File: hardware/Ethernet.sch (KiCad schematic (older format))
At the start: 25 parts

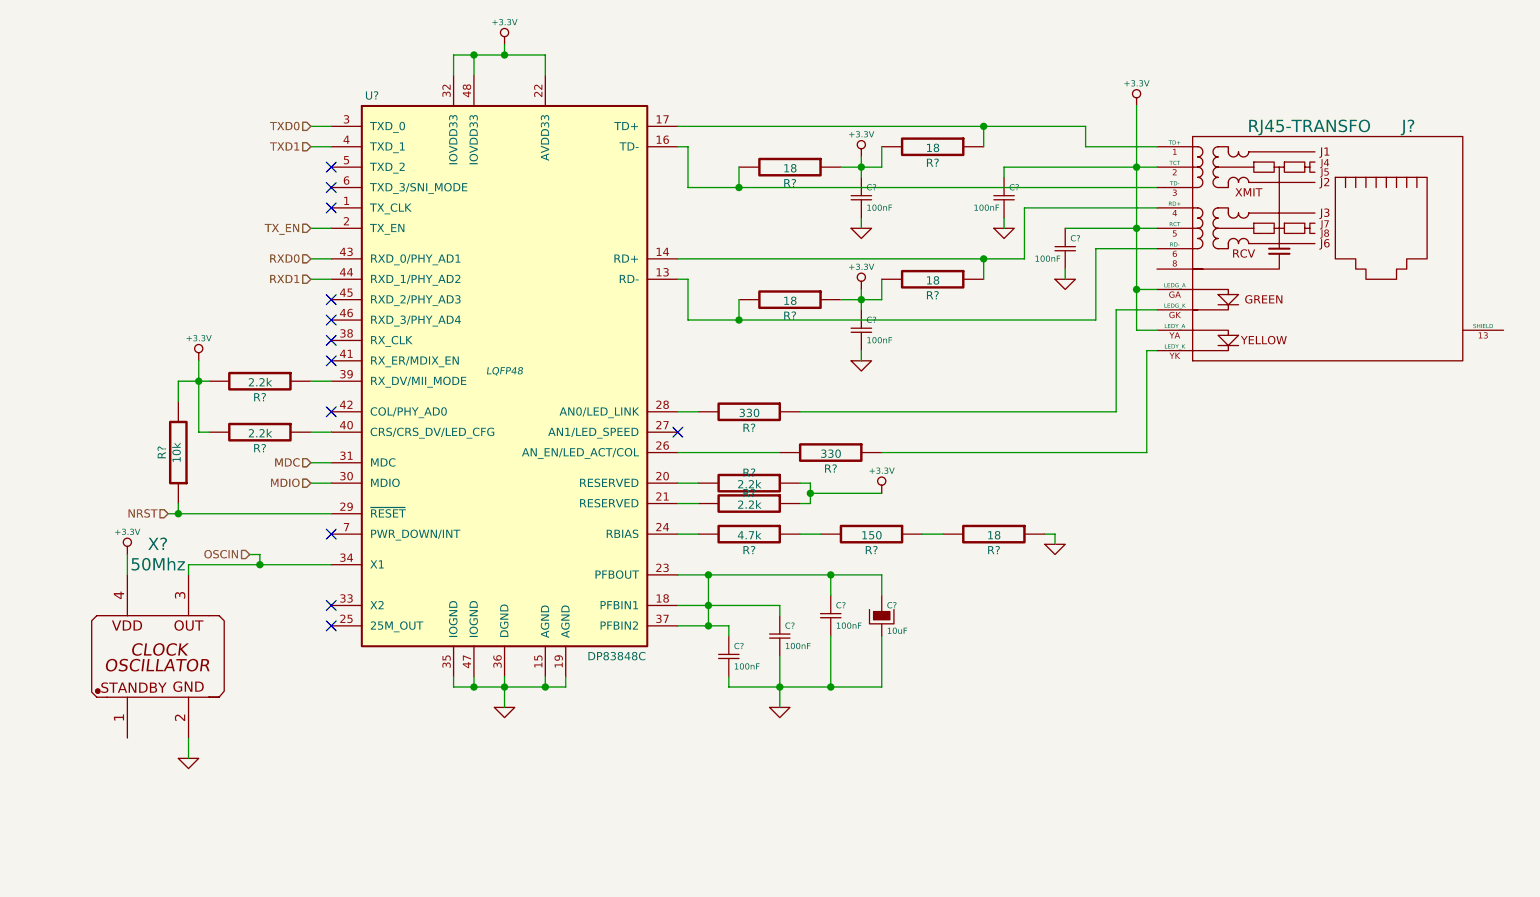
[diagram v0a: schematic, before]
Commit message: Se agrego alimentacion por USB-Serie, falta fuente
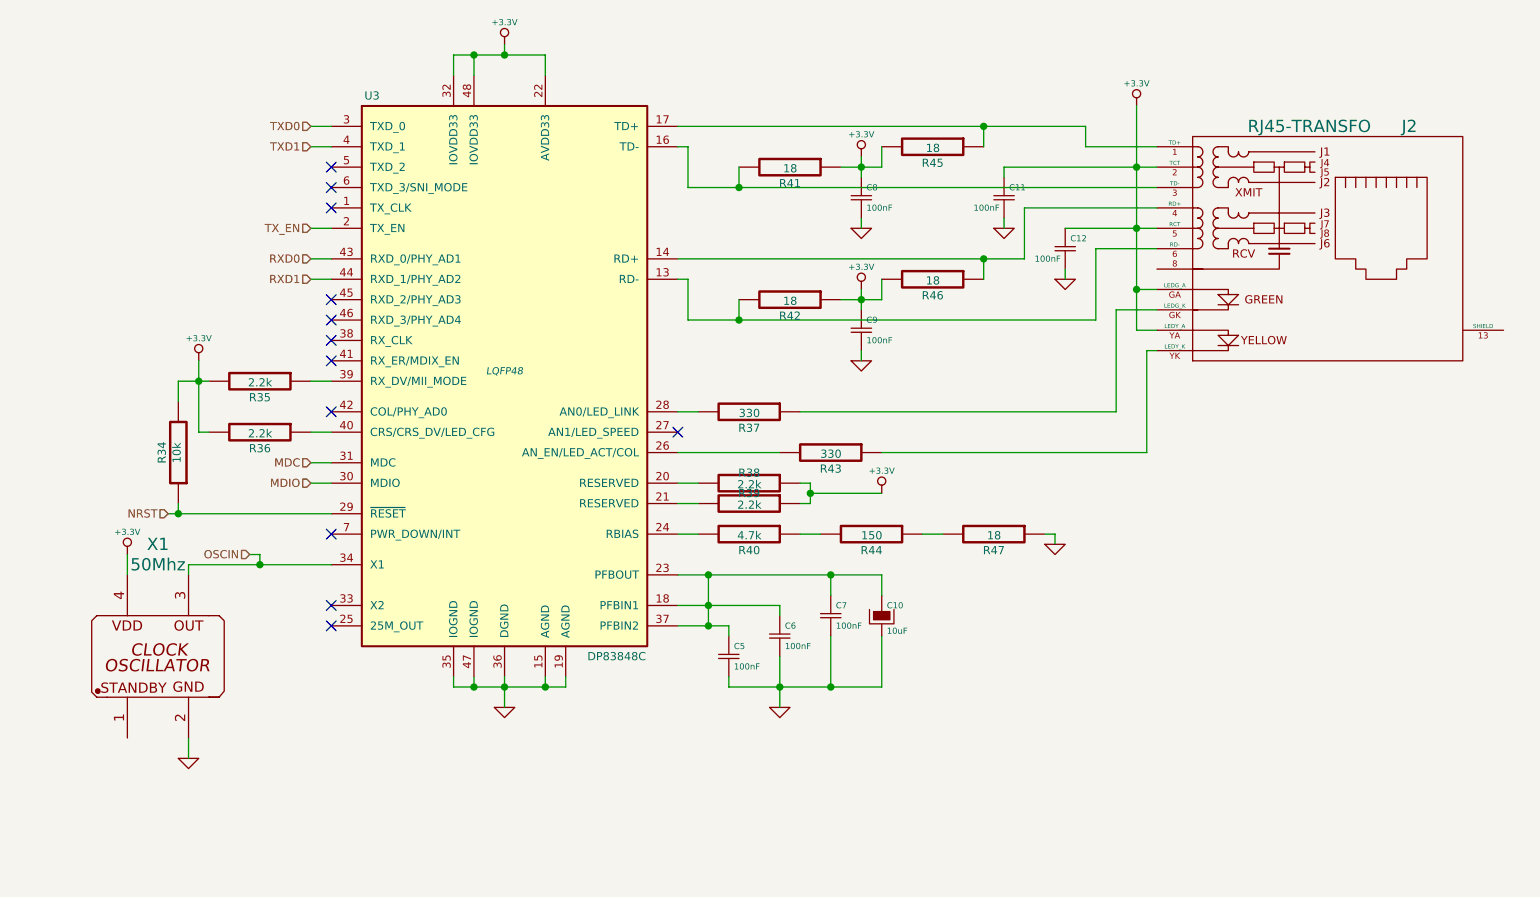
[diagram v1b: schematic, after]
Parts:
- gave numbers to parts that had none: 25
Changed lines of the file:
@@
 $Descr A4 11693 8268
 encoding utf-8
-Sheet 4 4
+Sheet 4 5
 Title ""
 Date ""
@@
 $EndDescr
 $Comp
-L DP83848C U?
+L DP83848C U3
 U 1 1 53947305
 P 4500 3600
-F 0 "U?" H 3850 4950 40  0000 C CNN
+F 0 "U3" H 3850 4950 40  0000 C CNN
 F 1 "DP83848C" H 5050 2200 40  0000 C CNN
 F 2 "LQFP48" H 4500 3600 35  0000 C CIN
@@
 $EndComp
 $Comp
-L R R?
+L R R40
 U 1 1 53947368
 P 5700 4400
-F 0 "R?" V 5780 4400 40  0000 C CNN
+F 0 "R40" V 5780 4400 40  0000 C CNN
 F 1 "4.7k" V 5707 4401 40  0000 C CNN
 F 2 "" V 5630 4400 30  0000 C CNN
@@
 $EndComp
 $Comp
-L R R?
+L R R44
 U 1 1 53947449
 P 6300 4400
-F 0 "R?" V 6380 4400 40  0000 C CNN
+F 0 "R44" V 6380 4400 40  0000 C CNN
 F 1 "150" V 6307 4401 40  0000 C CNN
 F 2 "" V 6230 4400 30  0000 C CNN
@@
 $EndComp
 $Comp
-L R R?
+L R R47
 U 1 1 53947480
 P 6900 4400
-F 0 "R?" V 6980 4400 40  0000 C CNN
+F 0 "R47" V 6980 4400 40  0000 C CNN
 F 1 "18" V 6907 4401 40  0000 C CNN
 F 2 "" V 6830 4400 30  0000 C CNN
@@
 	6550 4400 6650 4400
 $Comp
-L GND #PWR?
+L GND #PWR48
 U 1 1 539474DC
 P 7200 4450
-F 0 "#PWR?" H 7200 4450 30  0001 C CNN
+F 0 "#PWR48" H 7200 4450 30  0001 C CNN
 F 1 "GND" H 7200 4380 30  0001 C CNN
 F 2 "" H 7200 4450 60  0000 C CNN
@@
 	7200 4400 7150 4400
 $Comp
-L GND #PWR?
+L GND #PWR40
 U 1 1 53947528
 P 4500 5250
-F 0 "#PWR?" H 4500 5250 30  0001 C CNN
+F 0 "#PWR40" H 4500 5250 30  0001 C CNN
 F 1 "GND" H 4500 5180 30  0001 C CNN
 F 2 "" H 4500 5250 60  0000 C CNN
@@
 Connection ~ 4350 5150
 $Comp
-L +3.3V #PWR?
+L +3.3V #PWR39
 U 1 1 539475B5
 P 4500 2000
-F 0 "#PWR?" H 4500 1960 30  0001 C CNN
+F 0 "#PWR39" H 4500 1960 30  0001 C CNN
 F 1 "+3.3V" H 4500 2110 30  0000 C CNN
 F 2 "" H 4500 2000 60  0000 C CNN
@@
 Connection ~ 4500 2050
 $Comp
-L R R?
+L R R35
 U 1 1 5394763E
 P 3300 3650
-F 0 "R?" V 3380 3650 40  0000 C CNN
+F 0 "R35" V 3380 3650 40  0000 C CNN
 F 1 "2.2k" V 3307 3651 40  0000 C CNN
 F 2 "" V 3230 3650 30  0000 C CNN
@@
 	3550 3650 3650 3650
 $Comp
-L R R?
+L R R36
 U 1 1 539476E2
 P 3300 3900
-F 0 "R?" V 3380 3900 40  0000 C CNN
+F 0 "R36" V 3380 3900 40  0000 C CNN
 F 1 "2.2k" V 3307 3901 40  0000 C CNN
 F 2 "" V 3230 3900 30  0000 C CNN
@@
 Connection ~ 3000 3650
 $Comp
-L +3.3V #PWR?
+L +3.3V #PWR38
 U 1 1 53947762
 P 3000 3550
-F 0 "#PWR?" H 3000 3510 30  0001 C CNN
+F 0 "#PWR38" H 3000 3510 30  0001 C CNN
 F 1 "+3.3V" H 3000 3660 30  0000 C CNN
 F 2 "" H 3000 3550 60  0000 C CNN
@@
 	3550 2900 3650 2900
 $Comp
-L RJ45-TRANSFO J?
+L RJ45-TRANSFO J2
 U 1 1 539487CB
 P 8800 3000
-F 0 "J?" H 8900 3600 60  0000 L CNN
+F 0 "J2" H 8900 3600 60  0000 L CNN
 F 1 "RJ45-TRANSFO" H 8750 3600 60  0000 R CNN
 F 2 "" H 8800 3000 60  0000 C CNN
@@
 $EndComp
 $Comp
-L +3.3V #PWR?
+L +3.3V #PWR50
 U 1 1 53948AF2
 P 7600 2300
-F 0 "#PWR?" H 7600 2260 30  0001 C CNN
+F 0 "#PWR50" H 7600 2260 30  0001 C CNN
 F 1 "+3.3V" H 7600 2410 30  0000 C CNN
 F 2 "" H 7600 2300 60  0000 C CNN
@@
 	5400 2500 5350 2500
 $Comp
-L R R?
+L R R45
 U 1 1 53948C94
 P 6600 2500
-F 0 "R?" V 6680 2500 40  0000 C CNN
+F 0 "R45" V 6680 2500 40  0000 C CNN
 F 1 "18" V 6607 2501 40  0000 C CNN
 F 2 "" V 6530 2500 30  0000 C CNN
@@
 $EndComp
 $Comp
-L R R?
+L R R41
 U 1 1 53948D6C
 P 5900 2600
-F 0 "R?" V 5980 2600 40  0000 C CNN
+F 0 "R41" V 5980 2600 40  0000 C CNN
 F 1 "18" V 5907 2601 40  0000 C CNN
 F 2 "" V 5830 2600 30  0000 C CNN
@@
 Connection ~ 6850 2400
 $Comp
-L +3.3V #PWR?
+L +3.3V #PWR42
 U 1 1 53949005
 P 6250 2550
-F 0 "#PWR?" H 6250 2510 30  0001 C CNN
+F 0 "#PWR42" H 6250 2510 30  0001 C CNN
 F 1 "+3.3V" H 6250 2660 30  0000 C CNN
 F 2 "" H 6250 2550 60  0000 C CNN
@@
 $EndComp
 $Comp
-L Csmall C?
+L Csmall C8
 U 1 1 5394905D
 P 6250 2750
-F 0 "C?" H 6275 2800 30  0000 L CNN
+F 0 "C8" H 6275 2800 30  0000 L CNN
 F 1 "100nF" H 6275 2700 30  0000 L CNN
 F 2 "" H 6250 2750 60  0000 C CNN
@@
 $EndComp
 $Comp
-L GND #PWR?
+L GND #PWR43
 U 1 1 539490DB
 P 6250 2900
-F 0 "#PWR?" H 6250 2900 30  0001 C CNN
+F 0 "#PWR43" H 6250 2900 30  0001 C CNN
 F 1 "GND" H 6250 2830 30  0001 C CNN
 F 2 "" H 6250 2900 60  0000 C CNN
@@
 	6250 2900 6250 2850
 $Comp
-L R R?
+L R R46
 U 1 1 53949262
 P 6600 3150
-F 0 "R?" V 6680 3150 40  0000 C CNN
+F 0 "R46" V 6680 3150 40  0000 C CNN
 F 1 "18" V 6607 3151 40  0000 C CNN
 F 2 "" V 6530 3150 30  0000 C CNN
@@
 $EndComp
 $Comp
-L R R?
+L R R42
 U 1 1 53949268
 P 5900 3250
-F 0 "R?" V 5980 3250 40  0000 C CNN
+F 0 "R42" V 5980 3250 40  0000 C CNN
 F 1 "18" V 5907 3251 40  0000 C CNN
 F 2 "" V 5830 3250 30  0000 C CNN
@@
 Connection ~ 6850 3050
 $Comp
-L +3.3V #PWR?
+L +3.3V #PWR44
 U 1 1 53949275
 P 6250 3200
-F 0 "#PWR?" H 6250 3160 30  0001 C CNN
+F 0 "#PWR44" H 6250 3160 30  0001 C CNN
 F 1 "+3.3V" H 6250 3310 30  0000 C CNN
 F 2 "" H 6250 3200 60  0000 C CNN
@@
 $EndComp
 $Comp
-L Csmall C?
+L Csmall C9
 U 1 1 5394927D
 P 6250 3400
-F 0 "C?" H 6275 3450 30  0000 L CNN
+F 0 "C9" H 6275 3450 30  0000 L CNN
 F 1 "100nF" H 6275 3350 30  0000 L CNN
 F 2 "" H 6250 3400 60  0000 C CNN
@@
 $EndComp
 $Comp
-L GND #PWR?
+L GND #PWR45
 U 1 1 53949284
 P 6250 3550
-F 0 "#PWR?" H 6250 3550 30  0001 C CNN
+F 0 "#PWR45" H 6250 3550 30  0001 C CNN
 F 1 "GND" H 6250 3480 30  0001 C CNN
 F 2 "" H 6250 3550 60  0000 C CNN
@@
 	7400 3000 7700 3000
 $Comp
-L R R?
+L R R37
 U 1 1 539494A2
 P 5700 3800
-F 0 "R?" V 5780 3800 40  0000 C CNN
+F 0 "R37" V 5780 3800 40  0000 C CNN
 F 1 "330" V 5707 3801 40  0000 C CNN
 F 2 "" V 5630 3800 30  0000 C CNN
@@
 	7500 3300 7700 3300
 $Comp
-L R R?
+L R R43
 U 1 1 539495FE
 P 6100 4000
-F 0 "R?" V 6180 4000 40  0000 C CNN
+F 0 "R43" V 6180 4000 40  0000 C CNN
 F 1 "330" V 6107 4001 40  0000 C CNN
 F 2 "" V 6030 4000 30  0000 C CNN
@@
 NoConn ~ 5350 3900
 $Comp
-L R R?
+L R R38
 U 1 1 53949784
 P 5700 4150
-F 0 "R?" V 5650 4150 40  0000 C CNN
+F 0 "R38" V 5650 4150 40  0000 C CNN
 F 1 "2.2k" V 5707 4151 40  0000 C CNN
 F 2 "" V 5630 4150 30  0000 C CNN
@@
 $EndComp
 $Comp
-L R R?
+L R R39
 U 1 1 53949852
 P 5700 4250
-F 0 "R?" V 5650 4250 40  0000 C CNN
+F 0 "R39" V 5650 4250 40  0000 C CNN
 F 1 "2.2k" V 5707 4251 40  0000 C CNN
 F 2 "" V 5630 4250 30  0000 C CNN
@@
 	6000 4250 5950 4250
 $Comp
-L +3.3V #PWR?
+L +3.3V #PWR46
 U 1 1 53949A64
 P 6350 4200
-F 0 "#PWR?" H 6350 4160 30  0001 C CNN
+F 0 "#PWR46" H 6350 4160 30  0001 C CNN
 F 1 "+3.3V" H 6350 4310 30  0000 C CNN
 F 2 "" H 6350 4200 60  0000 C CNN
@@
 Connection ~ 5500 4750
 $Comp
-L Csmall C?
+L Csmall C5
 U 1 1 53949CA7
 P 5600 5000
-F 0 "C?" H 5625 5050 30  0000 L CNN
+F 0 "C5" H 5625 5050 30  0000 L CNN
 F 1 "100nF" H 5625 4950 30  0000 L CNN
 F 2 "" H 5600 5000 60  0000 C CNN
@@
 $EndComp
 $Comp
-L Csmall C?
+L Csmall C6
 U 1 1 53949D42
 P 5850 4900
-F 0 "C?" H 5875 4950 30  0000 L CNN
+F 0 "C6" H 5875 4950 30  0000 L CNN
 F 1 "100nF" H 5875 4850 30  0000 L CNN
 F 2 "" H 5850 4900 60  0000 C CNN
@@
 $EndComp
 $Comp
-L Csmall C?
+L Csmall C7
 U 1 1 53949D71
 P 6100 4800
-F 0 "C?" H 6125 4850 30  0000 L CNN
+F 0 "C7" H 6125 4850 30  0000 L CNN
 F 1 "100nF" H 6125 4750 30  0000 L CNN
 F 2 "" H 6100 4800 60  0000 C CNN
@@
 $EndComp
 $Comp
-L CPsmall C?
+L CPsmall C10
 U 1 1 5394A1E8
 P 6350 4800
-F 0 "C?" H 6375 4850 30  0000 L CNN
+F 0 "C10" H 6375 4850 30  0000 L CNN
 F 1 "10uF" H 6375 4725 30  0000 L CNN
 F 2 "" H 6350 4800 60  0000 C CNN
@@
 $EndComp
 $Comp
-L GND #PWR?
+L GND #PWR41
 U 1 1 5394A35A
 P 5850 5250
-F 0 "#PWR?" H 5850 5250 30  0001 C CNN
+F 0 "#PWR41" H 5850 5250 30  0001 C CNN
 F 1 "GND" H 5850 5180 30  0001 C CNN
 F 2 "" H 5850 5250 60  0000 C CNN
@@
 $EndComp
 $Comp
-L Csmall C?
+L Csmall C12
 U 1 1 5394A4D6
 P 7250 3000
-F 0 "C?" H 7275 3050 30  0000 L CNN
+F 0 "C12" H 7275 3050 30  0000 L CNN
 F 1 "100nF" H 7100 2950 30  0000 L CNN
 F 2 "" H 7250 3000 60  0000 C CNN
@@
 $EndComp
 $Comp
-L Csmall C?
+L Csmall C11
 U 1 1 5394A533
 P 6950 2750
-F 0 "C?" H 6975 2800 30  0000 L CNN
+F 0 "C11" H 6975 2800 30  0000 L CNN
 F 1 "100nF" H 6800 2700 30  0000 L CNN
 F 2 "" H 6950 2750 60  0000 C CNN
@@
 $EndComp
 $Comp
-L GND #PWR?
+L GND #PWR49
 U 1 1 5394A577
 P 7250 3150
-F 0 "#PWR?" H 7250 3150 30  0001 C CNN
+F 0 "#PWR49" H 7250 3150 30  0001 C CNN
 F 1 "GND" H 7250 3080 30  0001 C CNN
 F 2 "" H 7250 3150 60  0000 C CNN
@@
 	7250 3150 7250 3100
 $Comp
-L GND #PWR?
+L GND #PWR47
 U 1 1 5394A744
 P 6950 2900
-F 0 "#PWR?" H 6950 2900 30  0001 C CNN
+F 0 "#PWR47" H 6950 2900 30  0001 C CNN
 F 1 "GND" H 6950 2830 30  0001 C CNN
 F 2 "" H 6950 2900 60  0000 C CNN
@@
 Connection ~ 6250 3250
 $Comp
-L OSCILLATOR-VDD-4 X?
+L OSCILLATOR-VDD-4 X1
 U 1 1 5394BEE8
 P 2800 5000
-F 0 "X?" H 2800 5550 60  0000 C CNN
+F 0 "X1" H 2800 5550 60  0000 C CNN
 F 1 "50Mhz" H 2800 5450 60  0000 C CNN
 F 2 "" H 2800 5000 40  0000 C CNN
@@
 	2950 4550 3650 4550
 $Comp
-L +3.3V #PWR?
+L +3.3V #PWR36
 U 1 1 5394C114
 P 2650 4500
-F 0 "#PWR?" H 2650 4460 30  0001 C CNN
+F 0 "#PWR36" H 2650 4460 30  0001 C CNN
 F 1 "+3.3V" H 2650 4610 30  0000 C CNN
 F 2 "" H 2650 4500 60  0000 C CNN
@@
 	2650 4600 2650 4500
 $Comp
-L GND #PWR?
+L GND #PWR37
 U 1 1 5394C1B3
 P 2950 5500
-F 0 "#PWR?" H 2950 5500 30  0001 C CNN
+F 0 "#PWR37" H 2950 5500 30  0001 C CNN
 F 1 "GND" H 2950 5430 30  0001 C CNN
 F 2 "" H 2950 5500 60  0000 C CNN
@@
 	2950 5500 2950 5400
 $Comp
-L R R?
+L R R34
 U 1 1 5394C371
 P 2900 4000
-F 0 "R?" V 2980 4000 40  0000 C CNN
+F 0 "R34" V 2980 4000 40  0000 C CNN
 F 1 "10k" V 2907 4001 40  0000 C CNN
 F 2 "" V 2830 4000 30  0000 C CNN

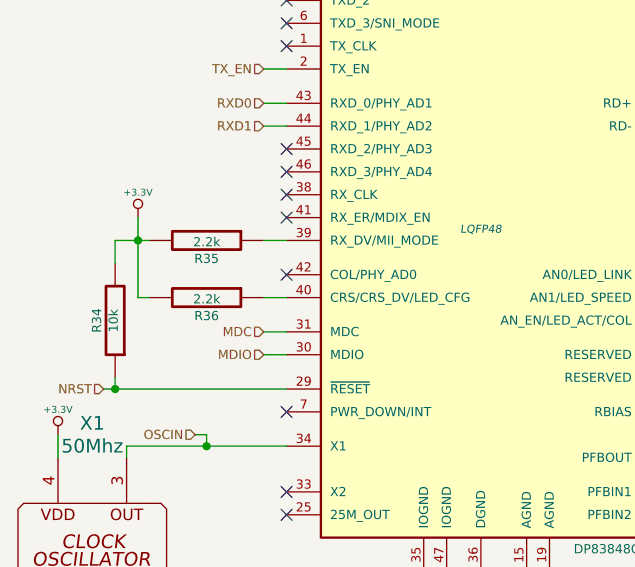
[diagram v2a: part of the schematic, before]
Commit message: Arreglada la distribucion de pines
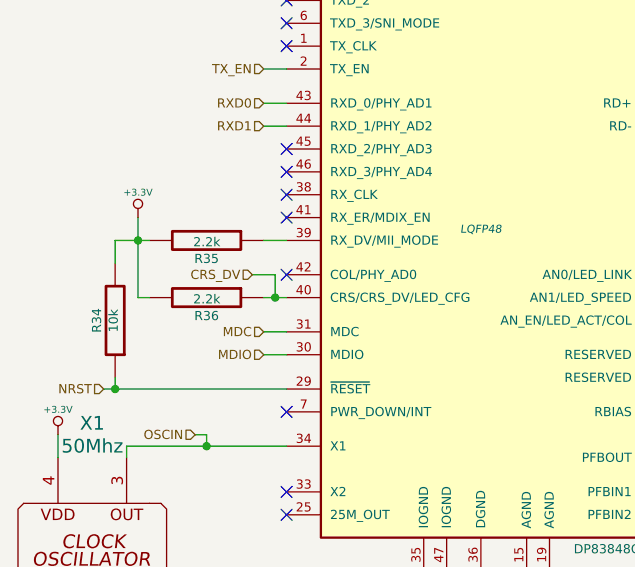
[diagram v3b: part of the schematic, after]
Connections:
- net CRS_DV: now reaches R36.1, U3.40 (CRS/CRS_DV/LED_CFG)
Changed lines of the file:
@@
 	3300 4500 3300 4550
 Connection ~ 3300 4550
+Text HLabel 3500 3800 0    40   Input ~ 0
+CRS_DV
+Wire Wire Line
+	3500 3800 3600 3800
+Wire Wire Line
+	3600 3800 3600 3900
+Connection ~ 3600 3900
 $EndSCHEMATC

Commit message: Terminado el esquematico, iniciado el PCB
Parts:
- added C21, C22, C23, C24: 100nF, Capacitors_SMD:c_1206, symbol Csmall
- C10: footprint (none) -> Capacitors_ThroughHole:Capacitor5x11RM2.5
- C11, C12, C5, C6, C7, C8, C9: footprint (none) -> Capacitors_SMD:c_1206
- R34, R35, R36, R37, R38, R39, R40, R41, R42, R43, R44, R45, R46, R47: footprint (none) -> Resistors_SMD:Resistor_SMD1206_ReflowWave
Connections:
- net +3.3V: now also C21.1, C22.1, C23.1, C24.1
- net GND: now also C21.2, C22.2, C23.2, C24.2
